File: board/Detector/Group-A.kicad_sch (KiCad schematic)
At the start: 27 parts, among them J1 Conn_02x04_Odd_Even, Q1 Q_Photo_NPN, Q2 Q_Photo_NPN, Q3 Q_Photo_NPN, Q4 Q_Photo_NPN, U1 LM339

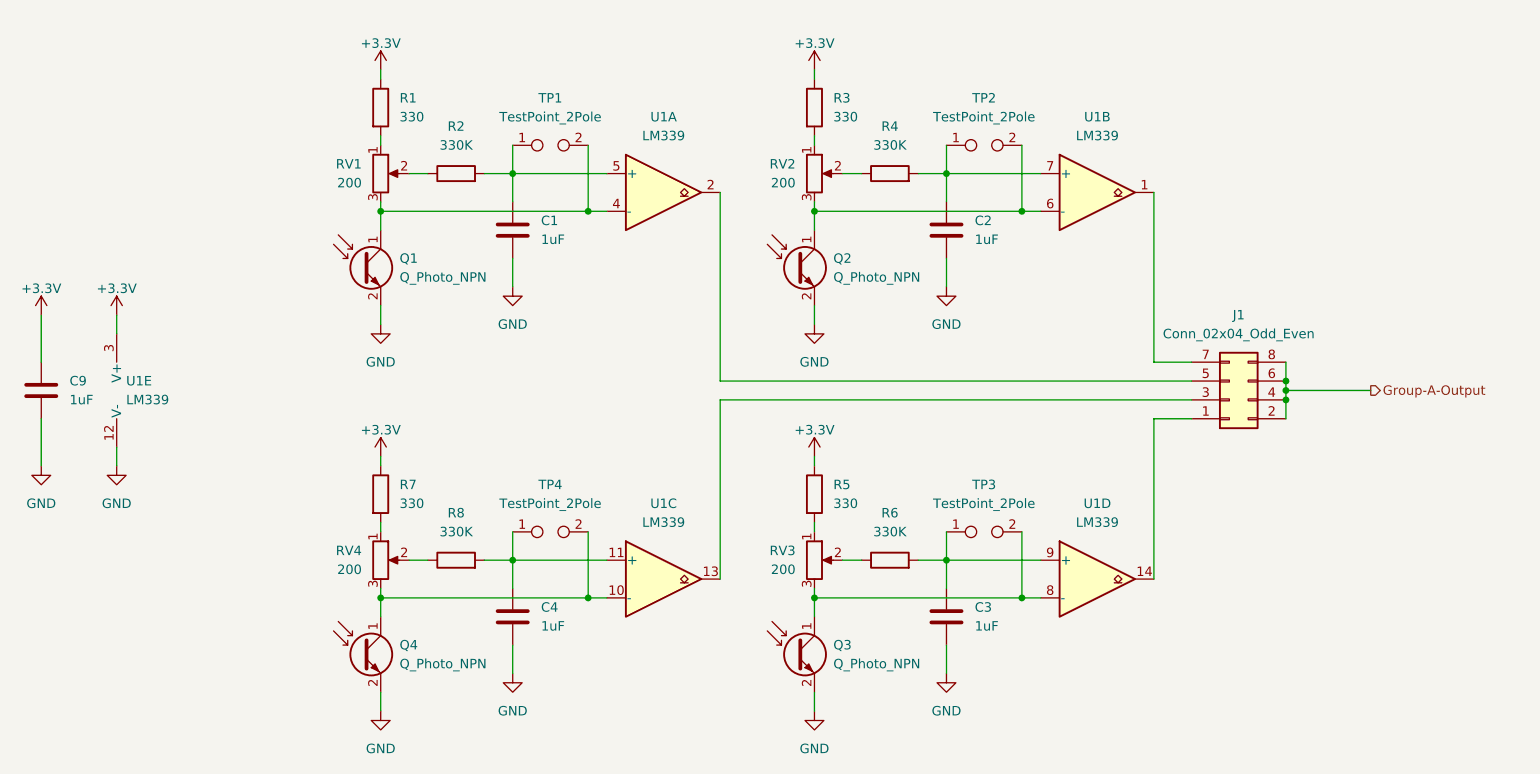
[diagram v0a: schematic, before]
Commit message: Fix the order of jumper links
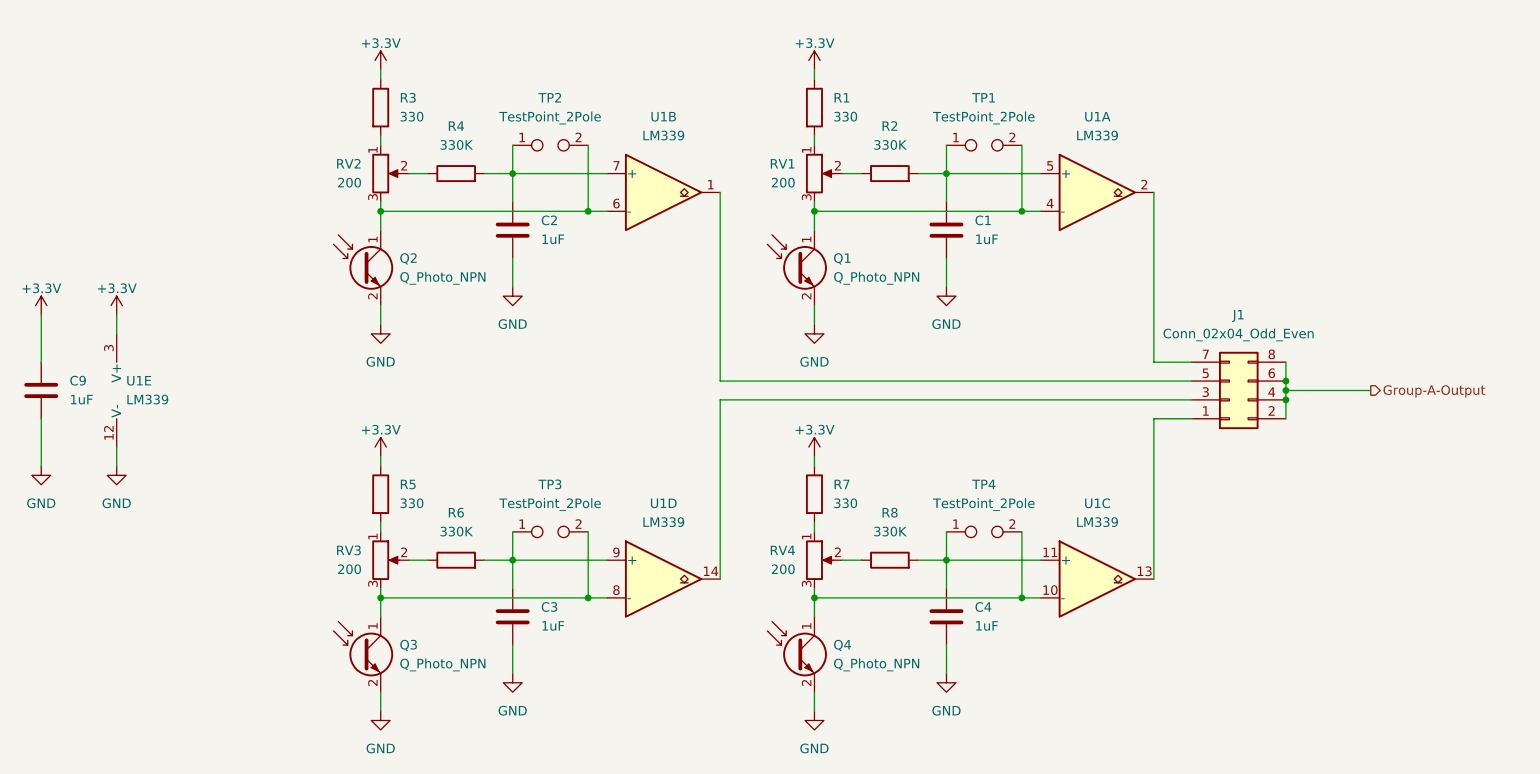
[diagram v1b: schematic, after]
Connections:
- net at J1.1 (Pin_1): now also U1.13; no longer U1.14
- net at J1.3 (Pin_3): now also U1.14; no longer U1.13
- net at J1.5 (Pin_5): now also U1.1; no longer U1.2
- net at J1.7 (Pin_7): now also U1.2; no longer U1.1
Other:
- moved on the sheet: C1, C2, C3, C4, Q1, Q2, Q3, Q4, R1, R2, R3, R4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

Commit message: Adjust values
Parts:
- Q1, Q2, Q3, Q4: value Q_Photo_NPN -> SFH 314 FA-2/3
- R1, R3, R5, R7: value 330 -> 2K
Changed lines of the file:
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@@
       (effects (font (size 1.27 1.27)) (justify left))
     )
-    (property "Value" "330" (id 1) (at 92.71 53.3399 0)
+    (property "Value" "2K" (id 1) (at 92.71 53.3399 0)
       (effects (font (size 1.27 1.27)) (justify left))
     )
@@
       (effects (font (size 1.27 1.27)) (justify left))
     )
-    (property "Value" "330" (id 1) (at 92.71 105.4099 0)
+    (property "Value" "2K" (id 1) (at 92.71 105.4099 0)
       (effects (font (size 1.27 1.27)) (justify left))
     )
@@
       (effects (font (size 1.27 1.27)) (justify left))
     )
-    (property "Value" "330" (id 1) (at 151.13 53.3399 0)
+    (property "Value" "2K" (id 1) (at 151.13 53.3399 0)
       (effects (font (size 1.27 1.27)) (justify left))
     )
@@
       (effects (font (size 1.27 1.27)) (justify left))
     )
-    (property "Value" "330" (id 1) (at 151.13 105.4099 0)
+    (property "Value" "2K" (id 1) (at 151.13 105.4099 0)
       (effects (font (size 1.27 1.27)) (justify left))
     )
@@
       (effects (font (size 1.27 1.27)) (justify left))
     )
-    (property "Value" "Q_Photo_NPN" (id 1) (at 92.71 74.9299 0)
+    (property "Value" "SFH 314 FA-2/3" (id 1) (at 92.71 74.9299 0)
       (effects (font (size 1.27 1.27)) (justify left))
     )
@@
       (effects (font (size 1.27 1.27)) (justify left))
     )
-    (property "Value" "Q_Photo_NPN" (id 1) (at 92.71 126.9999 0)
+    (property "Value" "SFH 314 FA-2/3" (id 1) (at 92.71 126.9999 0)
       (effects (font (size 1.27 1.27)) (justify left))
     )
@@
       (effects (font (size 1.27 1.27)) (justify left))
     )
-    (property "Value" "Q_Photo_NPN" (id 1) (at 151.13 74.9299 0)
+    (property "Value" "SFH 314 FA-2/3" (id 1) (at 151.13 74.9299 0)
       (effects (font (size 1.27 1.27)) (justify left))
     )
@@
       (effects (font (size 1.27 1.27)) (justify left))
     )
-    (property "Value" "Q_Photo_NPN" (id 1) (at 151.13 126.9999 0)
-      (effects (font (size 1.27 1.27)) (justify left))
-    )
+    (property "Value" "SFH 314 FA-2/3" (id 1) (at 151.13 126.9999 0)
+      (effects (font (size 1.27 1.27)) (justify left))
+    )

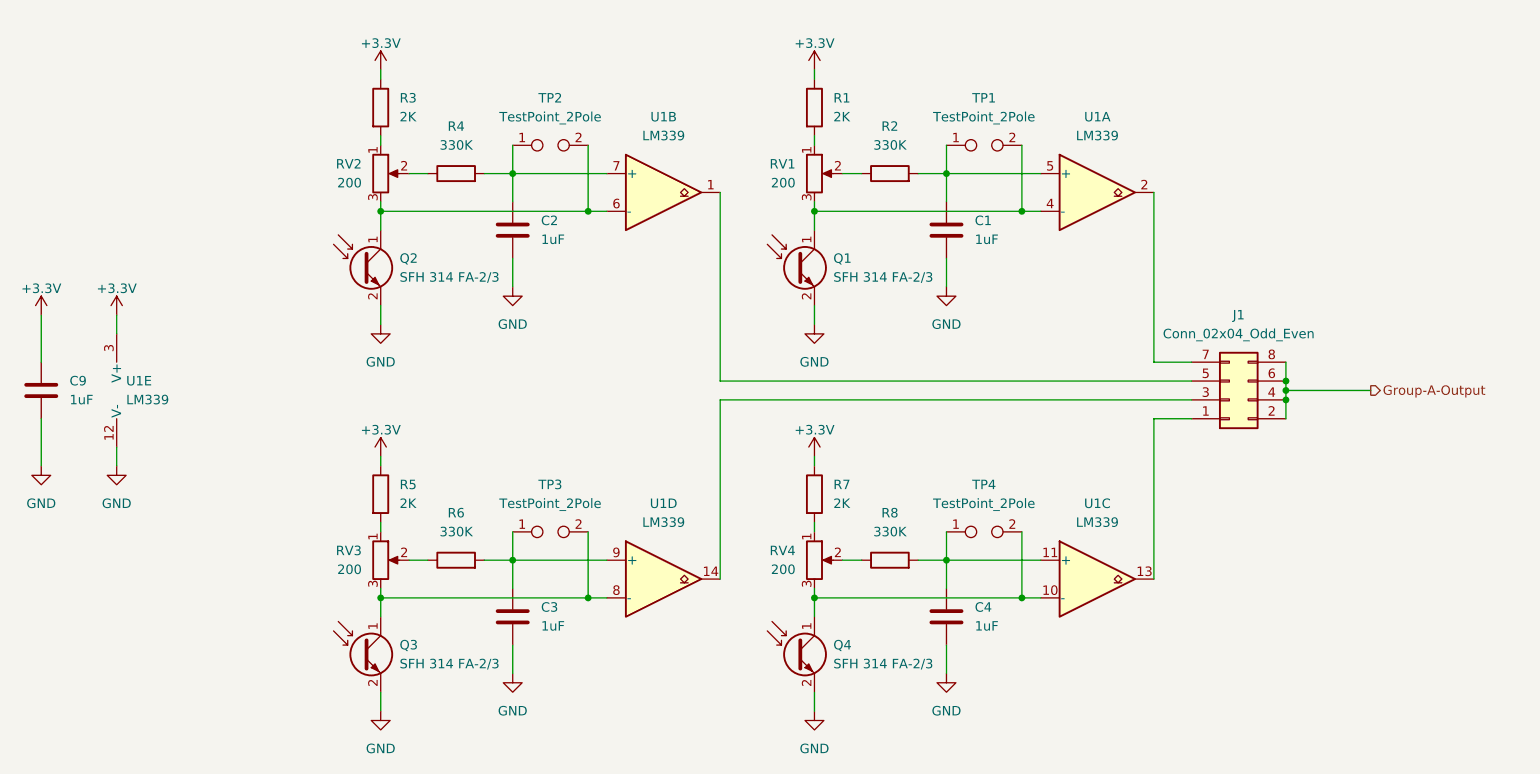
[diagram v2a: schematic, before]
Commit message: Detector changes to better control overall bias level
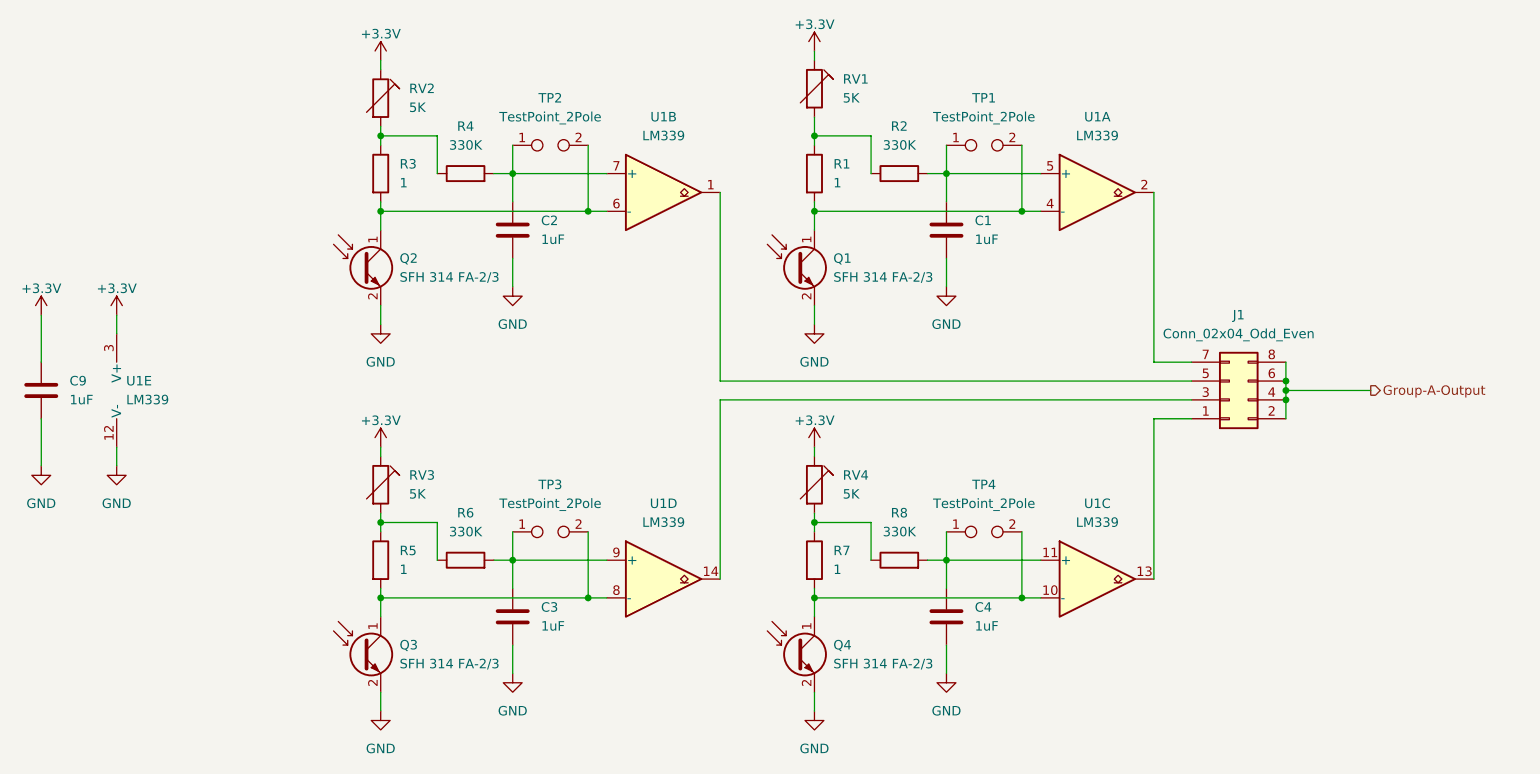
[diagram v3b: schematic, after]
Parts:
- removed RV1, RV2, RV3, RV4: 200, SamacSys_Parts:3362P_1, symbol Device:R_Potentiometer
- added RV1, RV2, RV3, RV4: 5K, SamacSys_Parts:3362P_1, symbol Device:R_Trim
- Q1, Q2, Q3, Q4: footprint LED_THT:LED_D3.0mm_Clear -> LED_THT:LED_D3.0mm_IRBlack
- R1, R3, R5, R7: value 2K -> 1
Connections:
- net +3V3: now also RV1.1, RV2.1, RV3.1, RV4.1; no longer R1.1, R3.1, R5.1, R7.1
- net at Q4.1 (C), TP4.2, U1.10 (-): now also R7.2
- net at R5.2: now also Q3.1 (C), TP3.2, U1.8 (-)
- net at R6.1: now also R5.1, RV3.2
- net at R4.1: now also R3.1, RV2.2
- net at R1.2: now also Q1.1 (C), TP1.2, U1.4 (-)
- net at R2.1: now also R1.1, RV1.2
- net at R8.1: now also R7.1, RV4.2
- net at R3.2: now also Q2.1 (C), TP2.2, U1.6 (-)
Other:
- moved on the sheet: R1, R2, R3, R4, R5, R6, R7, R8

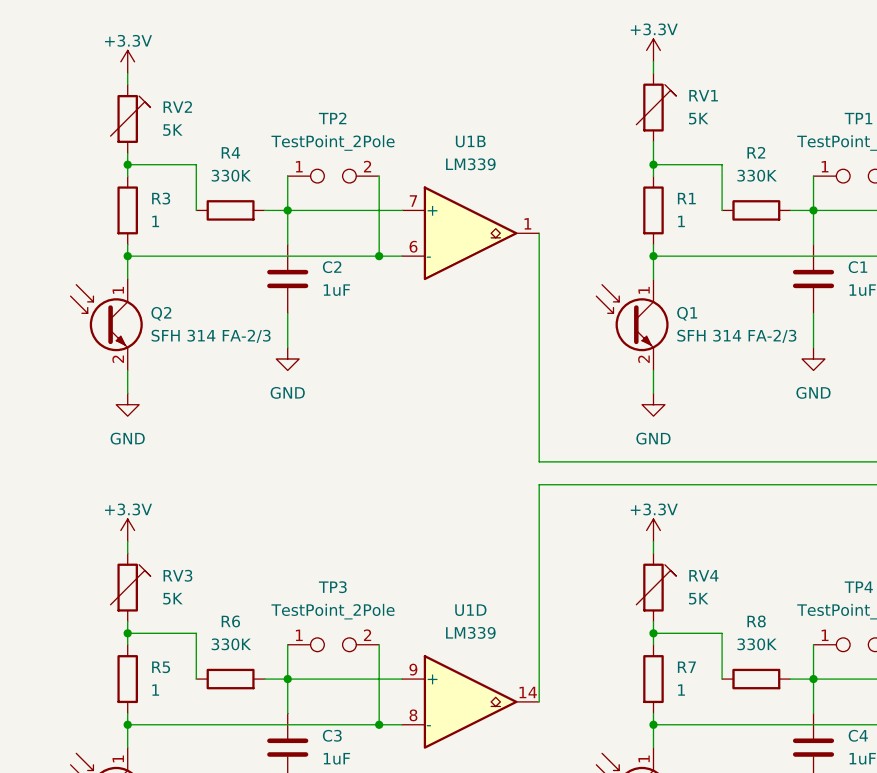
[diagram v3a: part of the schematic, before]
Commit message: Changed connectors, 3D models, added test points
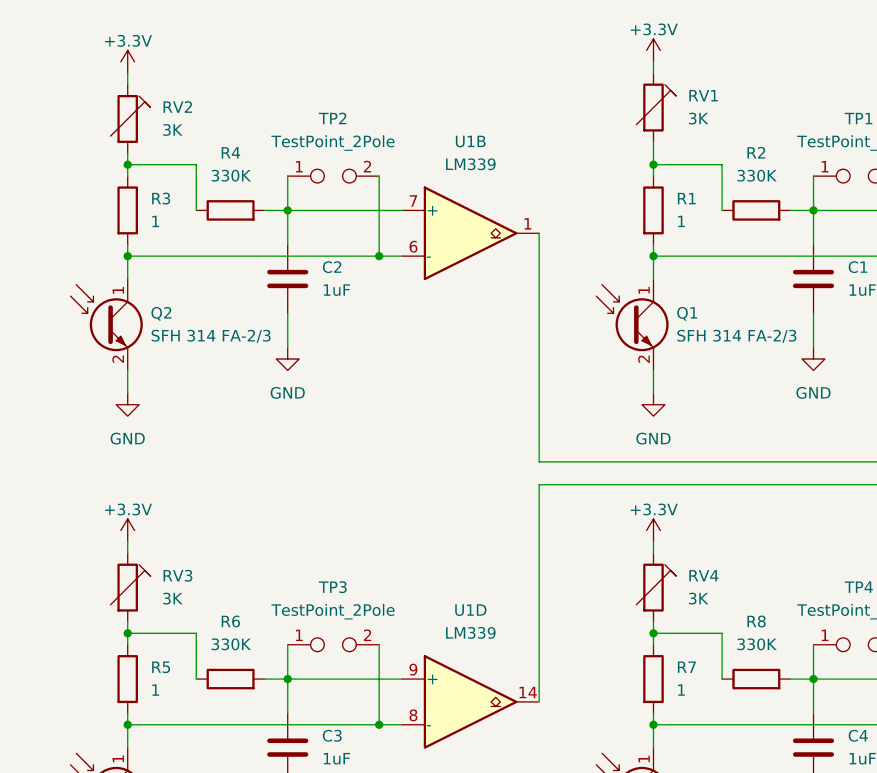
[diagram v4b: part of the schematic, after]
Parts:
- RV1, RV2, RV3, RV4: value 5K -> 3K

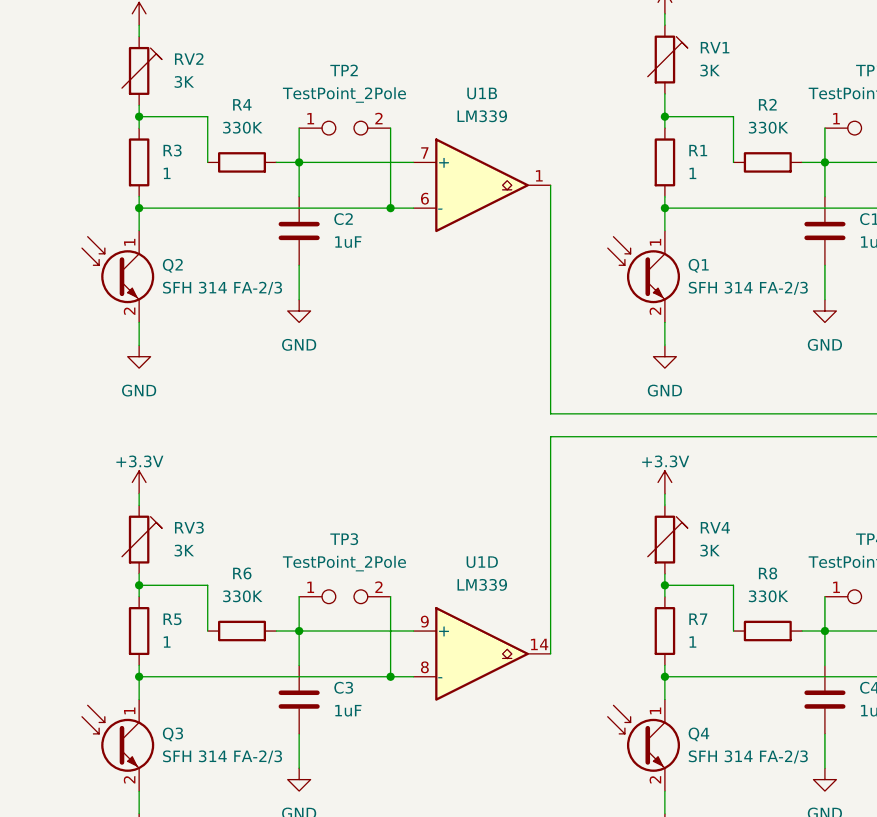
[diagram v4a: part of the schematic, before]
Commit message: Reduce sensitivity so we don't trigger on dust
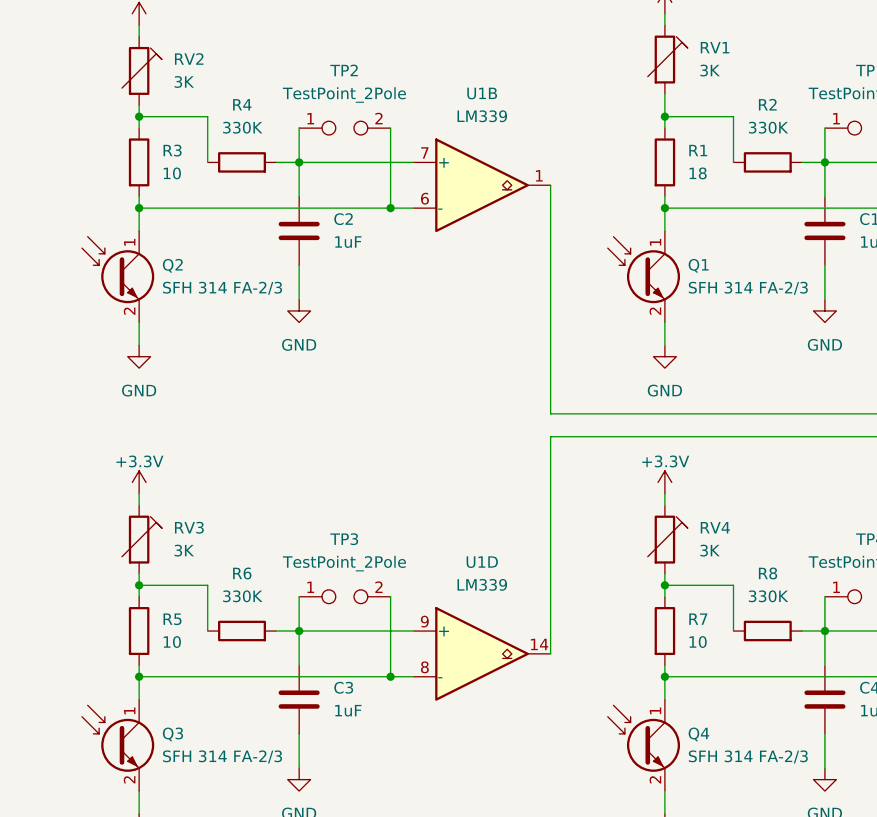
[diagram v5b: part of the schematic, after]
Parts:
- R1: value 1 -> 18
- R3, R5, R7: value 1 -> 10
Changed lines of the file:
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@@
       (effects (font (size 1.27 1.27)) hide)
     )
+    (pin "2")
+    (pin "4")
+    (pin "5")
+    (pin "1")
+    (pin "6")
+    (pin "7")
     (pin "10")
     (pin "11")
     (pin "13")
+    (pin "14")
+    (pin "8")
+    (pin "9")
+    (pin "12")
+    (pin "3")
   )
   (symbol (lib_id "Device:Q_Photo_NPN") (at 87.63 125.73 0) (unit 1)
@@
       (effects (font (size 1.27 1.27)) (justify left))
     )
-    (property "Value" "1" (id 1) (at 151.13 114.2999 0)
+    (property "Value" "10" (id 1) (at 151.13 114.2999 0)
       (effects (font (size 1.27 1.27)) (justify left))
     )
@@
       (effects (font (size 1.27 1.27)) hide)
     )
+    (pin "2")
+    (pin "4")
+    (pin "5")
+    (pin "1")
+    (pin "6")
+    (pin "7")
+    (pin "10")
+    (pin "11")
+    (pin "13")
+    (pin "14")
+    (pin "8")
+    (pin "9")
     (pin "12")
     (pin "3")
@@
       (effects (font (size 1.27 1.27)) hide)
     )
+    (pin "2")
+    (pin "4")
+    (pin "5")
+    (pin "1")
+    (pin "6")
+    (pin "7")
+    (pin "10")
+    (pin "11")
+    (pin "13")
     (pin "14")
     (pin "8")
     (pin "9")
+    (pin "12")
+    (pin "3")
   )
   (symbol (lib_id "power:+3.3V") (at 44.45 80.01 0) (unit 1)
@@
       (effects (font (size 1.27 1.27)) (justify left))
     )
-    (property "Value" "1" (id 1) (at 92.71 114.2999 0)
+    (property "Value" "10" (id 1) (at 92.71 114.2999 0)
       (effects (font (size 1.27 1.27)) (justify left))
     )
@@
       (effects (font (size 1.27 1.27)) (justify left))
     )
-    (property "Value" "1" (id 1) (at 92.71 62.2299 0)
+    (property "Value" "10" (id 1) (at 92.71 62.2299 0)
       (effects (font (size 1.27 1.27)) (justify left))
     )
@@
       (effects (font (size 1.27 1.27)) (justify left))
     )
-    (property "Value" "1" (id 1) (at 151.13 62.2299 0)
+    (property "Value" "18" (id 1) (at 151.13 62.2299 0)
       (effects (font (size 1.27 1.27)) (justify left))
     )
@@
       (effects (font (size 1.27 1.27)) hide)
     )
+    (pin "2")
+    (pin "4")
+    (pin "5")
     (pin "1")
     (pin "6")
     (pin "7")
+    (pin "10")
+    (pin "11")
+    (pin "13")
+    (pin "14")
+    (pin "8")
+    (pin "9")
+    (pin "12")
+    (pin "3")
   )
   (symbol (lib_id "power:GND") (at 166.37 128.27 0) (unit 1)
@@
     (pin "4")
     (pin "5")
+    (pin "1")
+    (pin "6")
+    (pin "7")
+    (pin "10")
+    (pin "11")
+    (pin "13")
+    (pin "14")
+    (pin "8")
+    (pin "9")
+    (pin "12")
+    (pin "3")
   )
   (symbol (lib_id "Device:Q_Photo_NPN") (at 146.05 73.66 0) (unit 1)
